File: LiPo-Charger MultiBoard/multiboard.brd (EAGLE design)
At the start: 50 x 50 mm, 25 parts, among them IC1 MCP73832T, IC2 MCP73832T

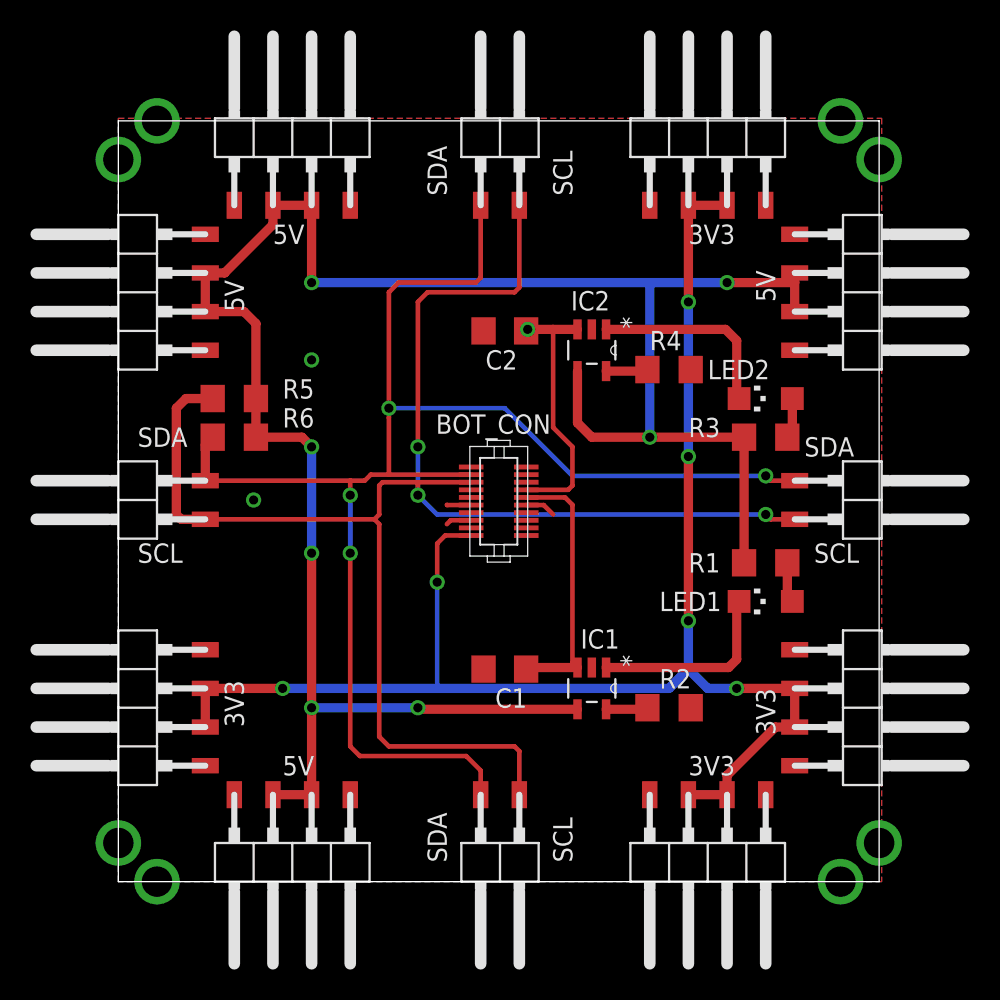
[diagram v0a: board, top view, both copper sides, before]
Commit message: Added Bot dimension to LiPo-Charger MultiBoard layout.
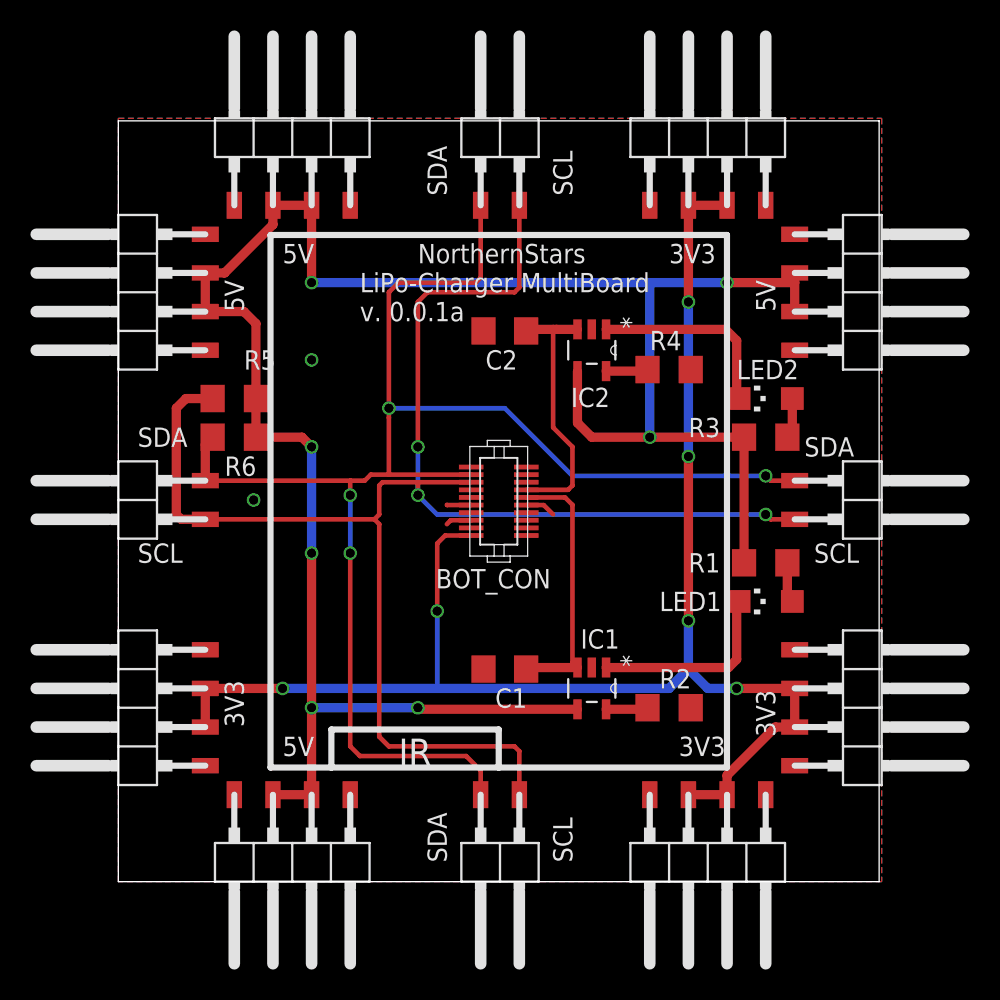
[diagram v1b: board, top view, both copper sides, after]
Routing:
- net BAT2: vias 1 -> 0
- net GND: vias 10 -> 2
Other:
- board text added: "IR"
- board text added: "LiPo-Charger MultiBoard"
- board text added: "NorthernStars"
- board text added: "v. 0.0.1a"
